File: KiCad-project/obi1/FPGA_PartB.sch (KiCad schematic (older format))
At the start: 10 parts, among them U3 XC6SLX16-FTG256

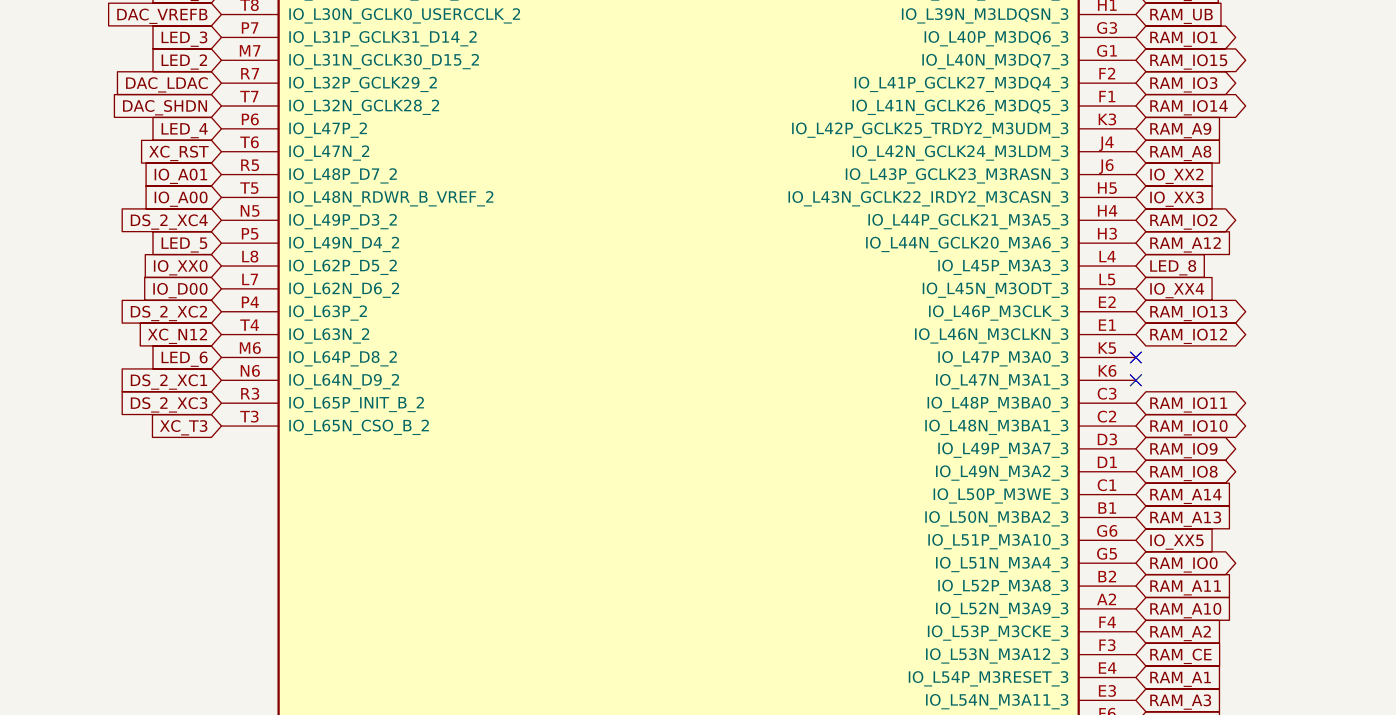
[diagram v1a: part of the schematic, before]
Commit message: Text in  Silk layer adjusted
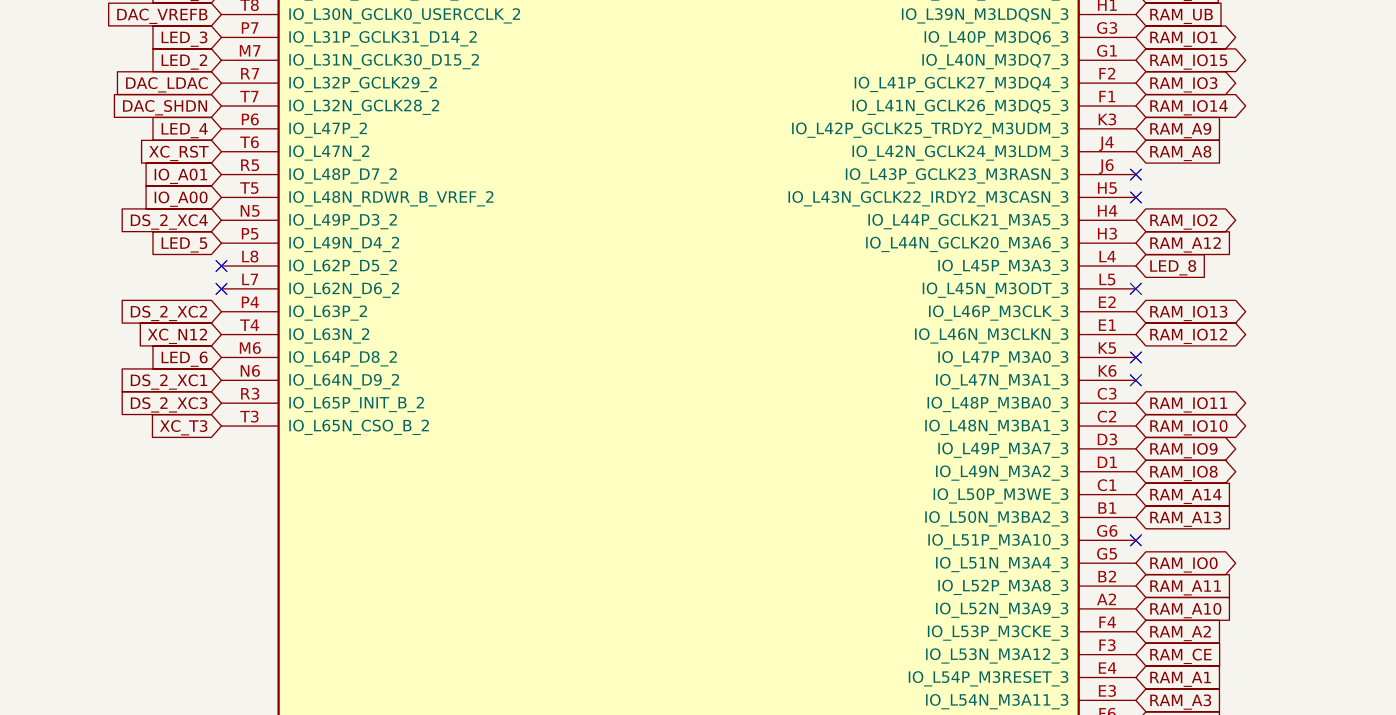
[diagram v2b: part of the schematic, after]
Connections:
- net labels removed: IO_D00, IO_XX0, IO_XX2, IO_XX3, IO_XX4, IO_XX5
- no-connect marks 5 -> 11
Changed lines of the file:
@@
 $Descr A4 11693 8268
 encoding utf-8
-Sheet 3 10
-Title ""
-Date ""
-Rev ""
-Comp ""
-Comment1 ""
-Comment2 ""
+Sheet 3 11
+Title "Spartan6 FTG256 Part B"
+Date "2021-04-08"
+Rev "0.2 "
+Comp "QRoboticsLab"
+Comment1 "by EGU"
+Comment2 "by JKGR"
 Comment3 ""
 Comment4 ""
@@
 Text GLabel 5450 6350 2    50   Input ~ 0
 RAM_A10
-Text GLabel 1450 4950 0    50   Input ~ 0
-IO_D00
 Text GLabel 1450 4350 0    50   Input ~ 0
 XC_RST
@@
 Text GLabel 5450 4850 2    50   Input ~ 0
 LED_8
-Text GLabel 5450 4450 2    50   Input ~ 0
-IO_XX2
-Text GLabel 5450 4550 2    50   Input ~ 0
-IO_XX3
-Text GLabel 5450 4950 2    50   Input ~ 0
-IO_XX4
-Text GLabel 5450 6050 2    50   Input ~ 0
-IO_XX5
 Wire Wire Line
 	1400 1050 1550 1050
@@
 Text GLabel 1450 3750 0    50   Input ~ 0
 DAC_VREFB
-Text GLabel 1450 4850 0    50   Input ~ 0
-IO_XX0
 Text GLabel 1450 4250 0    50   Input ~ 0
 LED_4
@@
 NoConn ~ 5450 5250
 NoConn ~ 5450 5350
+NoConn ~ 1450 4850
+NoConn ~ 1450 4950
+NoConn ~ 5450 4450
+NoConn ~ 5450 4550
+NoConn ~ 5450 4950
+NoConn ~ 5450 6050
 $EndSCHEMATC

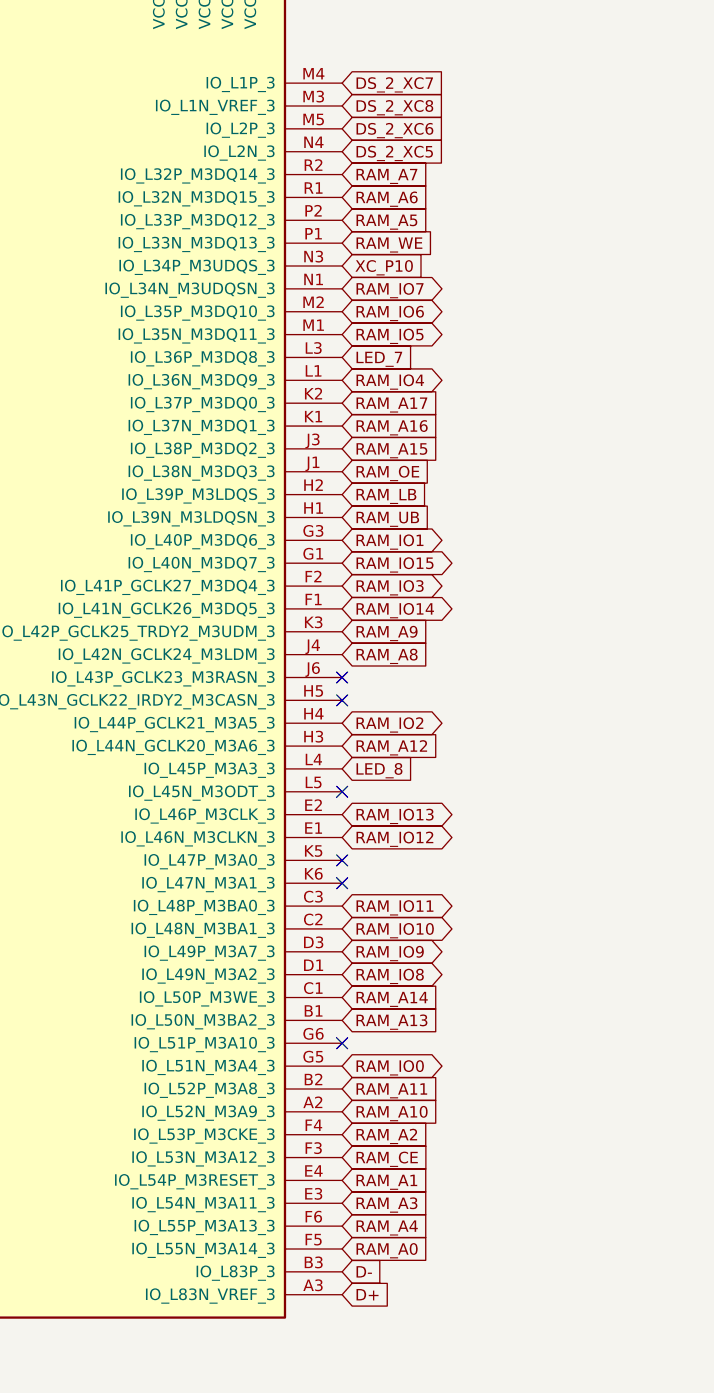
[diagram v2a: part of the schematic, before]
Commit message: Changed RAM by Cypres Model -rebuild symbolic and changed footprint
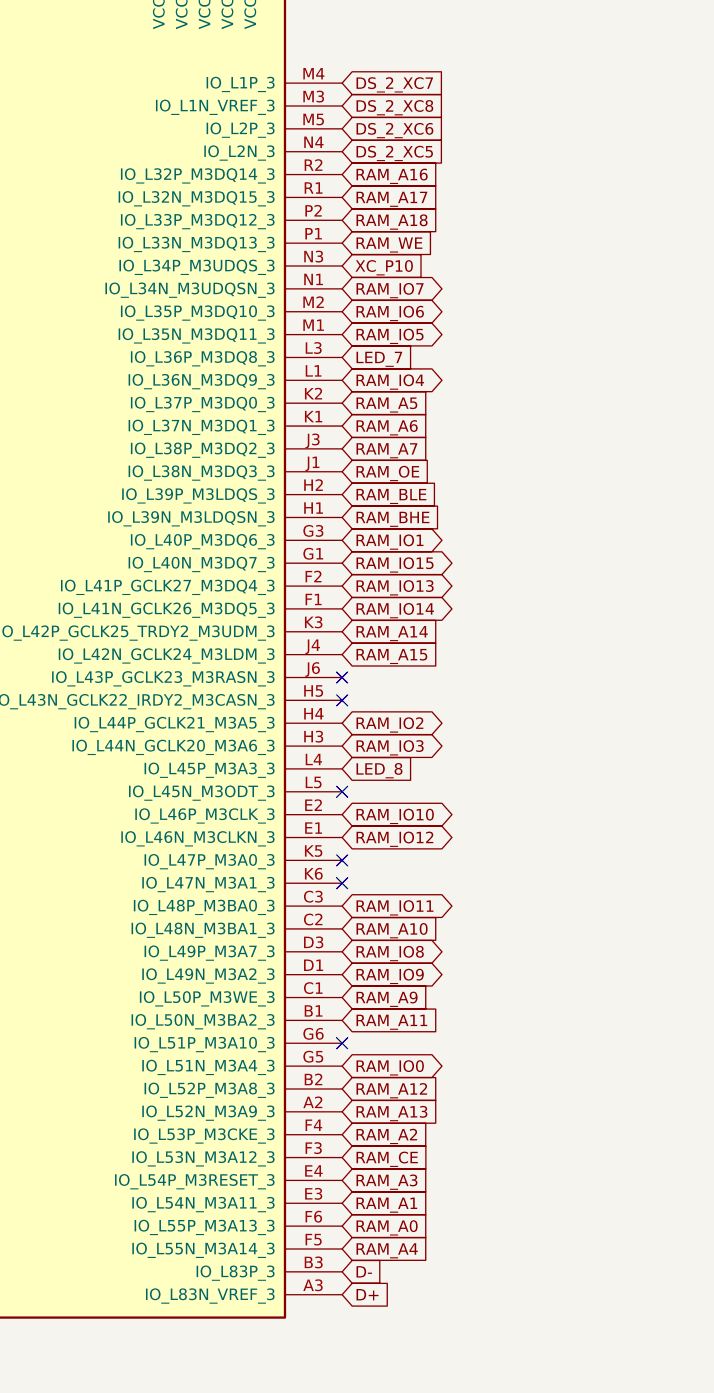
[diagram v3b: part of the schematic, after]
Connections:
- net labels added: RAM_A18, RAM_BHE, RAM_BLE
- net labels removed: RAM_A8, RAM_LB, RAM_UB
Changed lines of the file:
@@
 Text GLabel 1450 5550 0    50   Input ~ 0
 XC_T3
-Text GLabel 5450 6950 2    50   Input ~ 0
-RAM_A0
-Text GLabel 5450 6650 2    50   Input ~ 0
-RAM_A1
-Text GLabel 5450 6450 2    50   Input ~ 0
-RAM_A2
-Text GLabel 5450 6750 2    50   Input ~ 0
-RAM_A3
-Text GLabel 5450 6850 2    50   Input ~ 0
-RAM_A4
-Text GLabel 5450 6550 2    50   Input ~ 0
-RAM_CE
-Text GLabel 5450 3850 2    50   BiDi ~ 0
-RAM_IO1
-Text GLabel 5450 4650 2    50   BiDi ~ 0
-RAM_IO2
-Text GLabel 5450 4050 2    50   BiDi ~ 0
-RAM_IO3
-Text GLabel 5450 3150 2    50   BiDi ~ 0
-RAM_IO4
-Text GLabel 5450 2950 2    50   BiDi ~ 0
-RAM_IO5
-Text GLabel 5450 2850 2    50   BiDi ~ 0
-RAM_IO6
-Text GLabel 5450 2750 2    50   BiDi ~ 0
-RAM_IO7
-Text GLabel 5450 2550 2    50   Input ~ 0
-RAM_WE
-Text GLabel 5450 2450 2    50   Input ~ 0
-RAM_A5
-Text GLabel 5450 2350 2    50   Input ~ 0
-RAM_A6
-Text GLabel 5450 2250 2    50   Input ~ 0
-RAM_A7
-Text GLabel 5450 4350 2    50   Input ~ 0
-RAM_A8
-Text GLabel 5450 4250 2    50   Input ~ 0
-RAM_A9
-Text GLabel 5450 3250 2    50   Input ~ 0
-RAM_A17
-Text GLabel 5450 3350 2    50   Input ~ 0
-RAM_A16
-Text GLabel 5450 3450 2    50   Input ~ 0
-RAM_A15
-Text GLabel 5450 3550 2    50   Input ~ 0
-RAM_OE
-Text GLabel 5450 3750 2    50   Input ~ 0
-RAM_UB
-Text GLabel 5450 3650 2    50   Input ~ 0
-RAM_LB
-Text GLabel 5450 3950 2    50   BiDi ~ 0
-RAM_IO15
-Text GLabel 5450 4150 2    50   BiDi ~ 0
-RAM_IO14
-Text GLabel 5450 5050 2    50   BiDi ~ 0
-RAM_IO13
-Text GLabel 5450 5150 2    50   BiDi ~ 0
-RAM_IO12
-Text GLabel 5450 5450 2    50   BiDi ~ 0
-RAM_IO11
-Text GLabel 5450 5550 2    50   BiDi ~ 0
-RAM_IO10
-Text GLabel 5450 5650 2    50   BiDi ~ 0
-RAM_IO9
-Text GLabel 5450 5750 2    50   BiDi ~ 0
-RAM_IO8
-Text GLabel 5450 5850 2    50   Input ~ 0
-RAM_A14
-Text GLabel 5450 5950 2    50   Input ~ 0
-RAM_A13
-Text GLabel 5450 6250 2    50   Input ~ 0
-RAM_A11
-Text GLabel 5450 6350 2    50   Input ~ 0
-RAM_A10
 Text GLabel 1450 4350 0    50   Input ~ 0
 XC_RST
@@
 	1550 1250 1550 1050
 Connection ~ 1550 1050
-Text GLabel 5450 4750 2    50   Input ~ 0
-RAM_A12
-Text GLabel 5450 6150 2    50   BiDi ~ 0
-RAM_IO0
 Text GLabel 1450 3350 0    50   Input ~ 0
 DAC_CS
@@
 NoConn ~ 5450 4950
 NoConn ~ 5450 6050
+Text GLabel 5450 6850 2    50   Input ~ 0
+RAM_A0
+Text GLabel 5450 6750 2    50   Input ~ 0
+RAM_A1
+Text GLabel 5450 6450 2    50   Input ~ 0
+RAM_A2
+Text GLabel 5450 6650 2    50   Input ~ 0
+RAM_A3
+Text GLabel 5450 6950 2    50   Input ~ 0
+RAM_A4
+Text GLabel 5450 6550 2    50   Input ~ 0
+RAM_CE
+Text GLabel 5450 6150 2    50   BiDi ~ 0
+RAM_IO0
+Text GLabel 5450 3850 2    50   BiDi ~ 0
+RAM_IO1
+Text GLabel 5450 4650 2    50   BiDi ~ 0
+RAM_IO2
+Text GLabel 5450 3150 2    50   BiDi ~ 0
+RAM_IO4
+Text GLabel 5450 2950 2    50   BiDi ~ 0
+RAM_IO5
+Text GLabel 5450 2850 2    50   BiDi ~ 0
+RAM_IO6
+Text GLabel 5450 2750 2    50   BiDi ~ 0
+RAM_IO7
+Text GLabel 5450 2550 2    50   Input ~ 0
+RAM_WE
+Text GLabel 5450 4750 2    50   BiDi ~ 0
+RAM_IO3
+Text GLabel 5450 2350 2    50   Input ~ 0
+RAM_A17
+Text GLabel 5450 2250 2    50   Input ~ 0
+RAM_A16
+Text GLabel 5450 4350 2    50   Input ~ 0
+RAM_A15
+Text GLabel 5450 4250 2    50   Input ~ 0
+RAM_A14
+Text GLabel 5450 2450 2    50   Input ~ 0
+RAM_A18
+Text GLabel 5450 3250 2    50   Input ~ 0
+RAM_A5
+Text GLabel 5450 3350 2    50   Input ~ 0
+RAM_A6
+Text GLabel 5450 3450 2    50   Input ~ 0
+RAM_A7
+Text GLabel 5450 5850 2    50   Input ~ 0
+RAM_A9
+Text GLabel 5450 6250 2    50   Input ~ 0
+RAM_A12
+Text GLabel 5450 3550 2    50   Input ~ 0
+RAM_OE
+Text GLabel 5450 3750 2    50   Input ~ 0
+RAM_BHE
+Text GLabel 5450 5750 2    50   BiDi ~ 0
+RAM_IO9
+Text GLabel 5450 5650 2    50   BiDi ~ 0
+RAM_IO8
+Text GLabel 5450 6350 2    50   Input ~ 0
+RAM_A13
+Text GLabel 5450 5950 2    50   Input ~ 0
+RAM_A11
+Text GLabel 5450 5550 2    50   Input ~ 0
+RAM_A10
+Text GLabel 5450 5050 2    50   BiDi ~ 0
+RAM_IO10
+Text GLabel 5450 5450 2    50   BiDi ~ 0
+RAM_IO11
+Text GLabel 5450 5150 2    50   BiDi ~ 0
+RAM_IO12
+Text GLabel 5450 4050 2    50   BiDi ~ 0
+RAM_IO13
+Text GLabel 5450 4150 2    50   BiDi ~ 0
+RAM_IO14
+Text GLabel 5450 3950 2    50   BiDi ~ 0
+RAM_IO15
+Text GLabel 5450 3650 2    50   Input ~ 0
+RAM_BLE
 $EndSCHEMATC

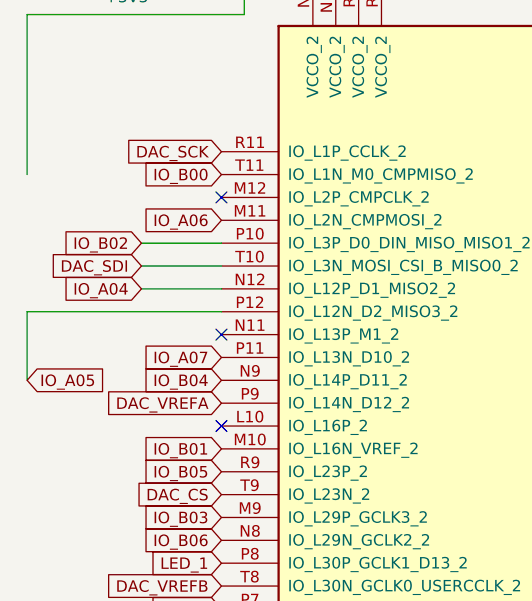
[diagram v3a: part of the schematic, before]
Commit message: IMU changed again, Final IMU= LSM6DSMTR, First Order to OSHPark
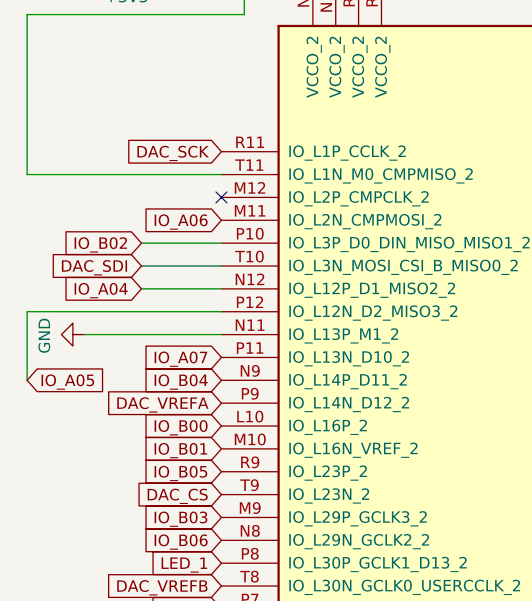
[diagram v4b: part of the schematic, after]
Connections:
- wire segments 38 -> 40
- no-connect marks 11 -> 9
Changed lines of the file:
@@
 Wire Wire Line
 	600  2550 1450 2550
-Wire Wire Line
-	5050 1050 4950 1050
-Connection ~ 4950 1050
-Wire Wire Line
-	4950 1050 4850 1050
-Connection ~ 4850 1050
-Wire Wire Line
-	4850 1050 4750 1050
-Connection ~ 4750 1050
-Wire Wire Line
-	4750 1050 4650 1050
-Wire Wire Line
-	4650 1050 4500 1050
-Connection ~ 4650 1050
-Wire Wire Line
-	2150 1050 2050 1050
-Connection ~ 2050 1050
-Wire Wire Line
-	2050 1050 1950 1050
-Connection ~ 1950 1050
-Wire Wire Line
-	1550 1050 1850 1050
-Wire Wire Line
-	1950 1050 1850 1050
-Connection ~ 1850 1050
-$Comp
-L FPGA_Xilinx_Spartan6:XC6SLX16-FTG256 U3
-U 2 1 5DA5D5E1
-P 3450 4150
-F 0 "U3" H 3450 950 50  0000 C CNN
-F 1 "XC6SLX16-FTG256" H 3450 850 50  0000 C CNN
-F 2 "Package_BGA:BGA-256_17.0x17.0mm_Layout16x16_P1.0mm_Ball0.5mm_Pad0.4mm_NSMD" H 3450 4150 50  0001 C CNN
-F 3 "" H 3450 4150 50  0000 C CNN
-	2    3450 4150
-	1    0    0    -1
-$EndComp
 Text GLabel 6250 1400 0    50   Input ~ 0
 XC_R11
@@
 Text GLabel 1450 3450 0    50   Input ~ 0
 IO_B03
-Text GLabel 1450 1950 0    50   Input ~ 0
-IO_B00
 Text GLabel 1450 3250 0    50   Input ~ 0
 IO_B05
 NoConn ~ 1450 2050
-NoConn ~ 1450 2650
-NoConn ~ 1450 3050
 NoConn ~ 5450 5250
 NoConn ~ 5450 5350
@@
 Text GLabel 5450 3650 2    50   Input ~ 0
 RAM_BLE
+Wire Wire Line
+	5050 1050 4950 1050
+Connection ~ 4950 1050
+Wire Wire Line
+	4950 1050 4850 1050
+Connection ~ 4850 1050
+Wire Wire Line
+	4850 1050 4750 1050
+Connection ~ 4750 1050
+Wire Wire Line
+	4750 1050 4650 1050
+Wire Wire Line
+	4650 1050 4500 1050
+Connection ~ 4650 1050
+Wire Wire Line
+	2150 1050 2050 1050
+Connection ~ 2050 1050
+Wire Wire Line
+	2050 1050 1950 1050
+Connection ~ 1950 1050
+Wire Wire Line
+	1550 1050 1850 1050
+Wire Wire Line
+	1950 1050 1850 1050
+Connection ~ 1850 1050
+$Comp
+L FPGA_Xilinx_Spartan6:XC6SLX16-FTG256 U3
+U 2 1 5DA5D5E1
+P 3450 4150
+F 0 "U3" H 3450 950 50  0000 C CNN
+F 1 "XC6SLX16-FTG256" H 3450 850 50  0000 C CNN
+F 2 "Package_BGA:BGA-256_17.0x17.0mm_Layout16x16_P1.0mm_Ball0.5mm_Pad0.4mm_NSMD" H 3450 4150 50  0001 C CNN
+F 3 "" H 3450 4150 50  0000 C CNN
+	2    3450 4150
+	1    0    0    -1
+$EndComp
+Text GLabel 1450 3050 0    50   Input ~ 0
+IO_B00
+Wire Wire Line
+	1450 1950 600  1950
+$Comp
+L power:GND #PWR0119
+U 1 1 60837234
+P 850 2650
+F 0 "#PWR0119" H 850 2400 50  0001 C CNN
+F 1 "GND" H 855 2477 50  0000 C CNN
+F 2 "" H 850 2650 50  0001 C CNN
+F 3 "" H 850 2650 50  0001 C CNN
+	1    850  2650
+	0    1    1    0
+$EndComp
+Wire Wire Line
+	850  2650 1450 2650
 $EndSCHEMATC
